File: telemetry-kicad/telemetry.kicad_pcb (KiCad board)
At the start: 4 copper layers, 0 parts

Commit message: Begun placement, need to make a footprint for the SD card module. All other footprints are loaded. Routing considerations are not input, such as the impidence controlled antenna trace.
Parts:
- added C1: 100nF, Capacitor_SMD:C_0805_2012Metric_Pad1.18x1.45mm_HandSolder, F.Cu at (128.3, 98.5)
- added C10: 1uF, Capacitor_SMD:C_0805_2012Metric_Pad1.18x1.45mm_HandSolder, F.Cu at (144.1, 98.5)
- added C12: 8pF, Capacitor_SMD:C_0805_2012Metric_Pad1.18x1.45mm_HandSolder, F.Cu at (123.2, 37.2)
- added C13: 8pF, Capacitor_SMD:C_0805_2012Metric_Pad1.18x1.45mm_HandSolder, F.Cu at (130.0, 44.5)
- added C15: 2.2uF, Capacitor_SMD:C_0805_2012Metric_Pad1.18x1.45mm_HandSolder, F.Cu at (172.2, 32.5)
- added C16: 2.2uF, Capacitor_SMD:C_0805_2012Metric_Pad1.18x1.45mm_HandSolder, F.Cu at (172.2, 35.5)
- added C17: 1uF, Capacitor_SMD:C_0805_2012Metric_Pad1.18x1.45mm_HandSolder, F.Cu at (132.5, 19.8)
- added C18: 1uF, Capacitor_SMD:C_0805_2012Metric_Pad1.18x1.45mm_HandSolder, F.Cu at (136.5, 19.7)
- added C19: 1uF, Capacitor_SMD:C_0805_2012Metric_Pad1.18x1.45mm_HandSolder, F.Cu at (140.5, 19.8)
- added C2: 10uF, Capacitor_SMD:C_0805_2012Metric_Pad1.18x1.45mm_HandSolder, F.Cu at (133.8, 98.5)
- added C20: 1uF, Capacitor_SMD:C_0805_2012Metric_Pad1.18x1.45mm_HandSolder, F.Cu at (144.5, 19.8)
- added C21: 1uF, Capacitor_SMD:C_0805_2012Metric_Pad1.18x1.45mm_HandSolder, F.Cu at (148.5, 19.8)
- added C22: 1uF, Capacitor_SMD:C_0805_2012Metric_Pad1.18x1.45mm_HandSolder, F.Cu at (152.5, 19.8)
- added C23: 10uF, Capacitor_SMD:C_0805_2012Metric_Pad1.18x1.45mm_HandSolder, F.Cu at (156.5, 19.8)
- added C24: 10uF, Capacitor_SMD:C_0805_2012Metric_Pad1.18x1.45mm_HandSolder, F.Cu at (160.4, 19.8)
- added C25: 10uF, Capacitor_SMD:C_0805_2012Metric_Pad1.18x1.45mm_HandSolder, F.Cu at (24.0, 112.0)
- added C26: 1uF, Capacitor_SMD:C_0805_2012Metric_Pad1.18x1.45mm_HandSolder, F.Cu at (28.0, 112.0)
- added C27: 1uF, Capacitor_SMD:C_0805_2012Metric_Pad1.18x1.45mm_HandSolder, F.Cu at (32.0, 112.0)
- added C28: 100nF, Capacitor_SMD:C_0805_2012Metric_Pad1.18x1.45mm_HandSolder, F.Cu at (52.8, 64.8)
- added C29: 100nF, Capacitor_SMD:C_0805_2012Metric_Pad1.18x1.45mm_HandSolder, F.Cu at (225.0, 45.8)
- added C3: 220nF, Capacitor_SMD:C_0805_2012Metric_Pad1.18x1.45mm_HandSolder, F.Cu at (138.6, 98.8)
- added C30: 10uF, Capacitor_SMD:C_0805_2012Metric_Pad1.18x1.45mm_HandSolder, F.Cu at (39.5, 112.0)
- added C31: 1uF, Capacitor_SMD:C_0805_2012Metric_Pad1.18x1.45mm_HandSolder, F.Cu at (43.5, 112.0)
- added C32: 1uF, Capacitor_SMD:C_0805_2012Metric_Pad1.18x1.45mm_HandSolder, F.Cu at (47.6, 112.0)
- added C33: 1uF, Capacitor_SMD:C_0805_2012Metric_Pad1.18x1.45mm_HandSolder, F.Cu at (210.0, 102.5)
- added C34: 100nF, Capacitor_SMD:C_0805_2012Metric_Pad1.18x1.45mm_HandSolder, F.Cu at (243.5, 79.0)
- added C5: 22uF, Capacitor_SMD:C_0805_2012Metric_Pad1.18x1.45mm_HandSolder, F.Cu at (129.1, 107.0)
- added C6: 22uF, Capacitor_SMD:C_0805_2012Metric_Pad1.18x1.45mm_HandSolder, F.Cu at (134.1, 107.0)
- added C7: 22uF, Capacitor_SMD:C_0805_2012Metric_Pad1.18x1.45mm_HandSolder, F.Cu at (138.6, 107.0)
- added C8: 10uF, Capacitor_SMD:C_0805_2012Metric_Pad1.18x1.45mm_HandSolder, F.Cu at (142.8, 107.0)
- added C9: 1uF, Capacitor_SMD:C_0805_2012Metric_Pad1.18x1.45mm_HandSolder, F.Cu at (147.1, 107.0)
- added D1: BZT52-C15S-AU_R1_000A1, Diode_SMD:D_SOD-123, F.Cu at (21.9, 53.5)
- added D2: D20V0L1B2LP-7B, Capacitor_SMD:C_0402_1005Metric_Pad0.74x0.62mm_HandSolder, F.Cu at (29.2, 49.0)
- added D4: PMEG2010BER, Diode_SMD:Nexperia_CFP3_SOD-123W, F.Cu at (103.8, 123.8)
- added F1: 1.5A Polyfuse, Inductor_SMD:L_1812_4532Metric_Pad1.30x3.40mm_HandSolder, F.Cu at (20.8, 45.8)
- added J1: 2601-1102, telemetry:WAGO-2601-1102, F.Cu at (38.5, 24.8)
- added J2: RFPC-SMA27-F, telemetry:RFPC-SMA27-F, F.Cu at (84.2, 23.8)
- added J4: 2601-1102, telemetry:WAGO-2601-1102, F.Cu at (50.9, 24.8)
- added J5: 2601-1102, telemetry:WAGO-2601-1102, F.Cu at (63.2, 24.8)
- added J6: USB_C_Receptacle_USB2.0_16P, telemetry:USB-C-SMD_TYPE-C-16PIN-2MD-073, F.Cu at (88.8, 124.4)
- added J8: TC2030, Connector:Tag-Connect_TC2030-IDC-NL_2x03_P1.27mm_Vertical, F.Cu at (60.6, 75.2)
- added L1: 8uH, 14m, Inductor_SMD:L_TaiTech_TMPC1265_13.5x12.5mm, F.Cu at (144.3, 87.0)
- added Q1: DMP3099LQ-7, Package_TO_SOT_SMD:SOT-23, F.Cu at (27.7, 42.2)
- added R1: 100k, Resistor_SMD:R_0805_2012Metric_Pad1.20x1.40mm_HandSolder, F.Cu at (154.1, 99.8)
- added R11: 10k, Resistor_SMD:R_0805_2012Metric_Pad1.20x1.40mm_HandSolder, F.Cu at (205.0, 119.0)
- added R12: 10k, Resistor_SMD:R_0805_2012Metric_Pad1.20x1.40mm_HandSolder, F.Cu at (205.0, 122.0)
- added R13: 10k, Resistor_SMD:R_0805_2012Metric_Pad1.20x1.40mm_HandSolder, F.Cu at (209.8, 110.2)
- added R14: 10k, Resistor_SMD:R_0805_2012Metric_Pad1.20x1.40mm_HandSolder, F.Cu at (209.8, 113.1)
- added R15: 10k, Resistor_SMD:R_0805_2012Metric_Pad1.20x1.40mm_HandSolder, F.Cu at (209.8, 116.0)
- added R16: 10k, Resistor_SMD:R_0805_2012Metric_Pad1.20x1.40mm_HandSolder, F.Cu at (209.8, 119.0)
- added R17: 5.1k, Resistor_SMD:R_0805_2012Metric_Pad1.20x1.40mm_HandSolder, F.Cu at (96.0, 111.2)
- added R18: 5.1k, Resistor_SMD:R_0805_2012Metric_Pad1.20x1.40mm_HandSolder, F.Cu at (95.9, 116.4)
- added R19: 10k, Resistor_SMD:R_0805_2012Metric_Pad1.20x1.40mm_HandSolder, F.Cu at (47.5, 65.8)
- added R2: 10K, Resistor_SMD:R_0805_2012Metric_Pad1.20x1.40mm_HandSolder, F.Cu at (21.0, 39.8)
- added R20: 10k, Resistor_SMD:R_0805_2012Metric_Pad1.20x1.40mm_HandSolder, F.Cu at (220.5, 38.8)
- added R21: 10k, Resistor_SMD:R_0805_2012Metric_Pad1.20x1.40mm_HandSolder, F.Cu at (214.5, 119.0)
- added R22: 10k, Resistor_SMD:R_0805_2012Metric_Pad1.20x1.40mm_HandSolder, F.Cu at (214.5, 122.0)
- added R23: 10k, Resistor_SMD:R_0805_2012Metric_Pad1.20x1.40mm_HandSolder, F.Cu at (220.5, 45.8)
- added R24: 10k, Resistor_SMD:R_0805_2012Metric_Pad1.20x1.40mm_HandSolder, F.Cu at (225.2, 38.8)
- added R25: 10k, Resistor_SMD:R_0805_2012Metric_Pad1.20x1.40mm_HandSolder, F.Cu at (248.8, 73.2)
- added R26: 10k, Resistor_SMD:R_0805_2012Metric_Pad1.20x1.40mm_HandSolder, F.Cu at (247.2, 93.5)
- added R27: 10k, Resistor_SMD:R_0805_2012Metric_Pad1.20x1.40mm_HandSolder, F.Cu at (248.8, 79.2)
- added R4: 43.2k, Resistor_SMD:R_0805_2012Metric_Pad1.20x1.40mm_HandSolder, F.Cu at (154.1, 105.8)
- added SW1: SW_NRST, telemetry:SMD-Switch, F.Cu at (53.3, 74.8)
- added SW2: SW_BOOT0, telemetry:SMD-Switch, F.Cu at (53.3, 79.0)
- added TP1: PG_BUCK, TestPoint:TestPoint_Pad_D1.0mm, F.Cu at (128.9, 88.5)
- added TP2: VBUS, TestPoint:TestPoint_Pad_D1.0mm, F.Cu at (125.5, 87.0)
- added TP3: +3V3, TestPoint:TestPoint_Pad_D1.0mm, F.Cu at (132.0, 88.5)
- added TP4: CANH1, TestPoint:TestPoint_Pad_D1.0mm, F.Cu at (221.2, 30.2)
- added TP5: CANL1, TestPoint:TestPoint_Pad_D1.0mm, F.Cu at (226.5, 30.2)
- added TP6: CANH2, TestPoint:TestPoint_Pad_D1.0mm, F.Cu at (241.2, 86.8)
- added TP7: CANL2, TestPoint:TestPoint_Pad_D1.0mm, F.Cu at (246.5, 86.8)
- added TP8: GND, TestPoint:TestPoint_Pad_D1.0mm, F.Cu at (33.5, 53.5)
- added U1: LMR33630ADDA, Package_SO:Texas_HSOP-8-1EP_3.9x4.9mm_P1.27mm_ThermalVias, F.Cu at (164.1, 92.1)
- added U2: TCAN337, Package_SO:SOIC-8_3.9x4.9mm_P1.27mm, F.Cu at (233.5, 38.2)
- added U3: TCAN337, Package_SO:SOIC-8_3.9x4.9mm_P1.27mm, F.Cu at (255.8, 87.0)
- added U4: ASM330LHHXG1TR, telemetry:ASM330LHHXG1TR, F.Cu at (27.8, 118.5)
- added U5: MAX-M10S-00B, telemetry:MAX-M10S-00B, F.Cu at (41.8, 124.2)
- added U7: STM32H523RCT7, telemetry:STM32H523RCT7, F.Cu at (146.5, 33.9)
- added U9: USBLC6-2SC6, Package_TO_SOT_SMD:SOT-23-6, F.Cu at (87.1, 112.3)
- added Y1: ABM8AIG-24.000MHz-8-2Z-T, telemetry:ABM8AIG-24.000MHZ-8-2Z-T, F.Cu at (129.7, 36.1)

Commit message: Progress on layout
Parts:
- moved C16 30.2 mm to (144.0, 24.8), turned to 90 degrees
- moved C24 27.8 mm to (144.8, 42.8), turned to -90 degrees
- moved C22 25.4 mm to (139.8, 41.8), turned to -90 degrees
- moved C15 25.4 mm to (149.2, 43.2), turned to -90 degrees
- moved C21 23.8 mm to (142.5, 42.8), turned to -90 degrees
- moved C20 23.0 mm to (153.2, 41.0)
- moved L1 20.2 mm to (163.8, 81.5), turned to 180 degrees
- moved C1 15.6 mm to (143.8, 101.0)
- moved C10 15.6 mm to (159.5, 101.0)
- moved C2 15.6 mm to (149.2, 101.0)
- moved C3 15.6 mm to (154.0, 101.2)
- moved C5 15.6 mm to (144.5, 109.5)
- moved C6 15.6 mm to (149.5, 109.5)
- moved C7 15.6 mm to (154.0, 109.5)
- moved C8 15.6 mm to (158.2, 109.5)
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
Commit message: Layout progress
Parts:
- moved C1 30.3 mm to (171.8, 89.5), turned to 90 degrees
- moved C5 27.3 mm to (152.0, 83.2), turned to 180 degrees
- moved C6 24.4 mm to (152.0, 85.2), turned to 180 degrees
- moved C7 22.3 mm to (152.0, 87.2), turned to 180 degrees
- moved C9 20.4 mm to (155.5, 90.3), turned to -90 degrees
- moved C8 19.9 mm to (153.2, 90.3), turned to 90 degrees
- moved TP1 17.3 mm to (143.4, 73.8)
- moved TP2 17.3 mm to (140.0, 72.2)
- moved TP3 17.3 mm to (146.5, 73.8)
- moved C10 14.4 mm to (172.0, 93.8)
- moved R4 12.6 mm to (165.8, 96.2), turned to 180 degrees
- moved C2 8.33 mm to (155.5, 95.5), turned to 90 degrees
- moved C3 6.86 mm to (157.8, 95.5), turned to 90 degrees
- moved R1 5.06 mm to (168.8, 97.2), turned to 90 degrees

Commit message: Routing progress
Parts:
- TP1, TP2, TP3, TP4, TP5, TP6, TP7, TP8: footprint TestPoint:TestPoint_Pad_D1.0mm -> TestPoint:TestPoint_THTPad_D2.0mm_Drill1.0mm
- moved U3 136.6 mm to (123.8, 51.5)
- moved R27 134.6 mm to (117.5, 49.0)
- moved C34 129.2 mm to (117.5, 52.5)
- moved TP6 126.5 mm to (121.0, 47.2)
- moved TP7 126.5 mm to (126.3, 47.2)
- moved R26 125.3 mm to (130.1, 49.2)
- moved R25 120.7 mm to (130.1, 53.0), turned to 180 degrees
- moved F1 118.8 mm to (120.2, 110.2), turned to -90 degrees
- moved R2 116.2 mm to (112.0, 112.0)
- moved D2 115.1 mm to (118.5, 116.8), turned to -90 degrees
- moved Q1 114.7 mm to (116.7, 114.5)
- moved D1 112.9 mm to (112.8, 115.8), turned to 90 degrees
- moved U2 109.8 mm to (123.8, 35.6)
- moved R24 106.8 mm to (117.5, 33.1)
- moved C29 106.6 mm to (117.5, 36.6)
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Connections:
- R23 pad 1: (no net) -> SIL_CAN1
- R23 pad 2: (no net) -> GND
- Y1 pad 2: (no net) -> GND
- Y1 pad 4: (no net) -> GND
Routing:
- net +3.3V: track 0.00 -> 57.0 mm
- net VBUS_USB: track 0.00 -> 14.7 mm, vias 0 -> 1
- net CYST_IN: track 0.00 -> 8.15 mm
- net CYST_OUT: track 0.00 -> 6.35 mm
- net Net-(U1-BOOT): track 0.00 -> 4.57 mm
- net /FB_BUCK: track 0.00 -> 4.25 mm
- net /VCC_BUCK: track 0.00 -> 4.13 mm
- net Net-(U1-PG): track 0.00 -> 3.67 mm
- net Net-(C15-Pad1): track 0.00 -> 2.75 mm
- net Net-(C16-Pad1): track 0.00 -> 2.57 mm
- added copper zone on F.Cu, net +3.3V
- added copper zone on F.Cu, net /SW_BUCK

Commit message: Routing Progressed, used Kicad MCP to make schematic for SD card
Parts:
- removed C32, C33: 1uF, Capacitor_SMD:C_0805_2012Metric_Pad1.18x1.45mm_HandSolder
- removed C34: 100nF, Capacitor_SMD:C_0805_2012Metric_Pad1.18x1.45mm_HandSolder
- removed D4: PMEG2010BER, Diode_SMD:Nexperia_CFP3_SOD-123W
- removed J8: TC2030, Connector:Tag-Connect_TC2030-IDC-NL_2x03_P1.27mm_Vertical
- removed R12, R13, R21, R22, R23, R24, R25, R26, R27: 10k, Resistor_SMD:R_0805_2012Metric_Pad1.20x1.40mm_HandSolder
- removed U9: USBLC6-2SC6, Package_TO_SOT_SMD:SOT-23-6
- added C11: 8pF, Capacitor_SMD:C_0805_2012Metric_Pad1.18x1.45mm_HandSolder, F.Cu at (88.5, 94.8)
- added C14: 2.2uF, Capacitor_SMD:C_0805_2012Metric_Pad1.18x1.45mm_HandSolder, F.Cu at (80.8, 108.2)
- added C4: 22uF, Capacitor_SMD:C_0805_2012Metric_Pad1.18x1.45mm_HandSolder, F.Cu at (118.5, 103.5)
- added D3: PMEG2010BER, Diode_SMD:Nexperia_CFP3_SOD-123W, F.Cu at (96.8, 124.8)
- added J3: TC2030, Connector:Tag-Connect_TC2030-IDC-NL_2x03_P1.27mm_Vertical, F.Cu at (77.5, 142.1)
- added J7: SD_Card_Receptacle, telemetry:SD_Yamaichi_FPS009-4200-0, F.Cu at (265.9, 119.0)
- added R10: 5.1k, Resistor_SMD:R_0805_2012Metric_Pad1.20x1.40mm_HandSolder, F.Cu at (83.5, 119.8)
- added R3: 43.2k, Resistor_SMD:R_0805_2012Metric_Pad1.20x1.40mm_HandSolder, F.Cu at (135.0, 117.8)
- added R5: 10k, Resistor_SMD:R_0805_2012Metric_Pad1.20x1.40mm_HandSolder, F.Cu at (22.2, 114.0)
- added R6: 10k, Resistor_SMD:R_0805_2012Metric_Pad1.20x1.40mm_HandSolder, F.Cu at (28.0, 114.0)
- added R7: 10k, Resistor_SMD:R_0805_2012Metric_Pad1.20x1.40mm_HandSolder, F.Cu at (41.8, 155.4)
- added R8: 10k, Resistor_SMD:R_0805_2012Metric_Pad1.20x1.40mm_HandSolder, F.Cu at (41.8, 158.4)
- added R9: 10k, Resistor_SMD:R_0805_2012Metric_Pad1.20x1.40mm_HandSolder, F.Cu at (41.8, 161.3)
- added U6: TCAN337, Package_SO:SOIC-8_3.9x4.9mm_P1.27mm, F.Cu at (48.4, 157.5)
- C10: value 1uF -> 100nF
- C13: value 8pF -> 100nF
- C16: value 2.2uF -> 100nF
- C23, C30, C8: value 10uF -> 1uF
- C26: value 1uF -> 10uF
- C28: value 100nF -> 1uF
- C29: value 100nF -> 10uF
- C7: value 22uF -> 10uF
- R11: value 10k -> 5.1k
- R17, R18: value 5.1k -> 10k
- R4: value 43.2k -> 10k
- TP1: value PG_BUCK -> VBUS
- TP2: value VBUS -> +3V3
- TP3: value +3V3 -> PG_BUCK
- TP4: value CANH1 -> GND
- TP5: value CANL1 -> CANH1
- TP6: value CANH2 -> CANL1
- TP7: value CANL2 -> CANH2
- TP8: value GND -> CANL2
- U2: value TCAN337 -> ASM330LHHXG1TR; footprint Package_SO:SOIC-8_3.9x4.9mm_P1.27mm -> telemetry:ASM330LHHXG1TR
- U3: value TCAN337 -> MAX-M10S-00B; footprint Package_SO:SOIC-8_3.9x4.9mm_P1.27mm -> telemetry:MAX-M10S-00B
- U4: value ASM330LHHXG1TR -> TCAN337; footprint telemetry:ASM330LHHXG1TR -> Package_SO:SOIC-8_3.9x4.9mm_P1.27mm
- U5: value MAX-M10S-00B -> STM32H523RCT7; footprint telemetry:MAX-M10S-00B -> telemetry:STM32H523RCT7
- U7: value STM32H523RCT7 -> USBLC6-2SC6; footprint telemetry:STM32H523RCT7 -> Package_TO_SOT_SMD:SOT-23-6
- moved R19 201.7 mm to (221.8, 126.5)
- moved C26 156.4 mm to (162.8, 35.8)
- moved C27 153.0 mm to (161.8, 27.0)
- moved C28 150.4 mm to (167.5, 29.8)
- moved R4 139.8 mm to (26.0, 100.5)
- moved R17 137.0 mm to (222.0, 109.5), turned to 0 degrees
- moved C10 136.5 mm to (35.2, 101.8)
- moved R18 130.0 mm to (221.8, 129.0), turned to 0 degrees
- moved C17 129.3 mm to (221.8, 119.5), turned to 180 degrees
- moved R11 111.8 mm to (93.2, 119.8)
- moved R20 105.9 mm to (28.8, 68.2)
- moved C30 98.3 mm to (113.5, 72.5)
- moved C31 98.3 mm to (113.5, 70.2)
- moved C16 82.2 mm to (22.0, 68.2)
- moved C13 74.2 mm to (59.5, 157.0)
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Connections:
- C10 pad 1: /VCC_BUCK -> GND
- C10 pad 2: GND -> +3.3V
- C12 pad 1: CYST_OUT -> CYST_IN
- C13 pad 1: CYST_IN -> GND
- C13 pad 2: GND -> +3.3V
- C16 pad 1: Net-(C16-Pad1) -> NRST
- C25 pad 1: GND -> +3.3V
- C25 pad 2: +3.3V -> GND
- C26 pad 1: +3.3V -> GND
- C26 pad 2: GND -> +3.3V
- C28 pad 1: NRST -> +3.3V
- C30 pad 1: GND -> +3.3V
- C30 pad 2: +3.3V -> GND
- C7 pad 1: +3.3V -> GND
- C7 pad 2: GND -> +3.3V
- C8 pad 1: GND -> +3.3V
- C8 pad 2: +3.3V -> GND
- C9 pad 1: +3.3V -> /VCC_BUCK
- J4 pad 1: Net-(J4-1_1) -> /CANH1
- J4 pad 2: Net-(J4-1_1) -> /CANH1
- J4 pad 3: Net-(J4-2_1) -> /CANL1
- J4 pad 4: Net-(J4-2_1) -> /CANL1
- J5 pad 1: Net-(J5-1_1) -> /CANH2
- J5 pad 2: Net-(J5-1_1) -> /CANH2
- J5 pad 3: Net-(J5-2_1) -> /CANL2
- J5 pad 4: Net-(J5-2_1) -> /CANL2
- R11 pad 1: +3.3V -> Net-(J6-CC2)
- R11 pad 2: CMD_SD -> GND
- R14 pad 2: D2_SD -> CMD_SD
- R15 pad 2: D1_SD -> CLK_SD
- R16 pad 2: D0_SD -> D3_SD
- R17 pad 1: Net-(J6-CC1) -> +3.3V
- R17 pad 2: GND -> D2_SD
- R18 pad 1: Net-(J6-CC2) -> +3.3V
- R18 pad 2: GND -> D1_SD
- R19 pad 1: Net-(U7A-BOOT0) -> +3.3V
- R19 pad 2: GND -> D0_SD
- R20 pad 1: +3.3V -> Net-(U5A-BOOT0)
- R20 pad 2: FLT_CAN1 -> GND
- R4 pad 1: /FB_BUCK -> +3.3V
- R4 pad 2: GND -> TXD_CAN1
- SW2 pad 1: Net-(U7A-BOOT0) -> Net-(U5A-BOOT0)
- TP1 pad 1: Net-(U1-PG) -> VBUS_USB
- TP2 pad 1: VBUS_USB -> +3.3V
- TP3 pad 1: +3.3V -> Net-(U1-PG)
- TP4 pad 1: Net-(J4-1_1) -> GND
- TP5 pad 1: Net-(J4-2_1) -> /CANH1
- TP6 pad 1: Net-(J5-1_1) -> /CANL1
- TP7 pad 1: Net-(J5-2_1) -> /CANH2
- TP8 pad 1: GND -> /CANL2
- U2 pad 1: TXD_CAN1 -> DO_IMU
- U2 pad 3: +3.3V -> GND
- U2 pad 4: RXD_CAN1 -> INT1
- U2 pad 5: FLT_CAN1 -> +3.3V
- U2 pad 6: Net-(J4-2_1) -> GND
- U2 pad 7: Net-(J4-1_1) -> GND
- U2 pad 8: SIL_CAN1 -> +3.3V
- U3 pad 1: TXD_CAN2 -> GND
- U3 pad 2: GND -> TXD_GNSS
- U3 pad 3: +3.3V -> RXD_GNSS
- U3 pad 4: RXD_CAN2 -> TIMEPULSE_GNSS
- U3 pad 5: FLT_CAN2 -> unconnected-(U3-EXTINT-Pad5)
- U3 pad 6: Net-(J5-2_1) -> unconnected-(U3-V_BCKP-Pad6)
- U3 pad 7: Net-(J5-1_1) -> +3.3V
- U3 pad 8: SIL_CAN2 -> +3.3V
- U4 pad 1: DO_IMU -> TXD_CAN1
- U4 pad 3: GND -> +3.3V
- U4 pad 4: INT1 -> RXD_CAN1
- U4 pad 5: +3.3V -> FLT_CAN1
- U4 pad 6: GND -> /CANL1
- U4 pad 7: GND -> /CANH1
- U4 pad 8: +3.3V -> SIL_CAN1
- U5 pad 1: GND -> +3.3V
- U5 pad 10: GND -> unconnected-(U5A-PC2-Pad10)
- U5 pad 11: ANT -> unconnected-(U5A-PC3-Pad11)
- U5 pad 13: unconnected-(U5-LNA_EN-Pad13) -> +3.3V
- U5 pad 18: unconnected-(U5-~{SAFEBOOT}-Pad18) -> GND
- U5 pad 2: TXD_GNSS -> unconnected-(U5A-PC13-Pad2)
- U5 pad 3: RXD_GNSS -> unconnected-(U5A-PC14-OSC32_IN-Pad3)
- U5 pad 4: TIMEPULSE_GNSS -> unconnected-(U5A-PC15-OSC32_OUT-Pad4)
- U5 pad 5: unconnected-(U5-EXTINT-Pad5) -> CYST_IN
- U5 pad 6: unconnected-(U5-V_BCKP-Pad6) -> CYST_OUT
- U5 pad 7: +3.3V -> NRST
- U5 pad 8: +3.3V -> unconnected-(U5A-PC0-Pad8)
- U7 pad 1: +3.3V -> /inD-
- U7 pad 2: unconnected-(U7A-PC13-Pad2) -> GND
- U7 pad 3: unconnected-(U7A-PC14-OSC32_IN-Pad3) -> /inD+
- U7 pad 4: unconnected-(U7A-PC15-OSC32_OUT-Pad4) -> D+
- U7 pad 5: CYST_IN -> /VBUS
- U7 pad 6: CYST_OUT -> D-
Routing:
- net /VBUS: track 0.00 -> 26.7 mm
- net Net-(D2-A1): track 0.00 -> 8.81 mm
- net +3.3V: track 57.0 -> 48.8 mm
- net VBUS_USB: track 14.7 -> 22.7 mm
- net Net-(D1-A): track 0.00 -> 7.74 mm
- net /inD-: track 0.00 -> 6.30 mm
- net /inD+: track 0.00 -> 6.26 mm
- net D-: track 0.00 -> 6.16 mm
- net D+: track 0.00 -> 5.35 mm
- net Net-(J6-CC1): track 0.00 -> 4.41 mm, vias 0 -> 2
- net Net-(J6-CC2): track 0.00 -> 3.85 mm, vias 0 -> 2
- net Net-(C16-Pad1): track 2.57 -> 0.00 mm
- net Net-(C14-Pad1): track 0.00 -> 2.52 mm

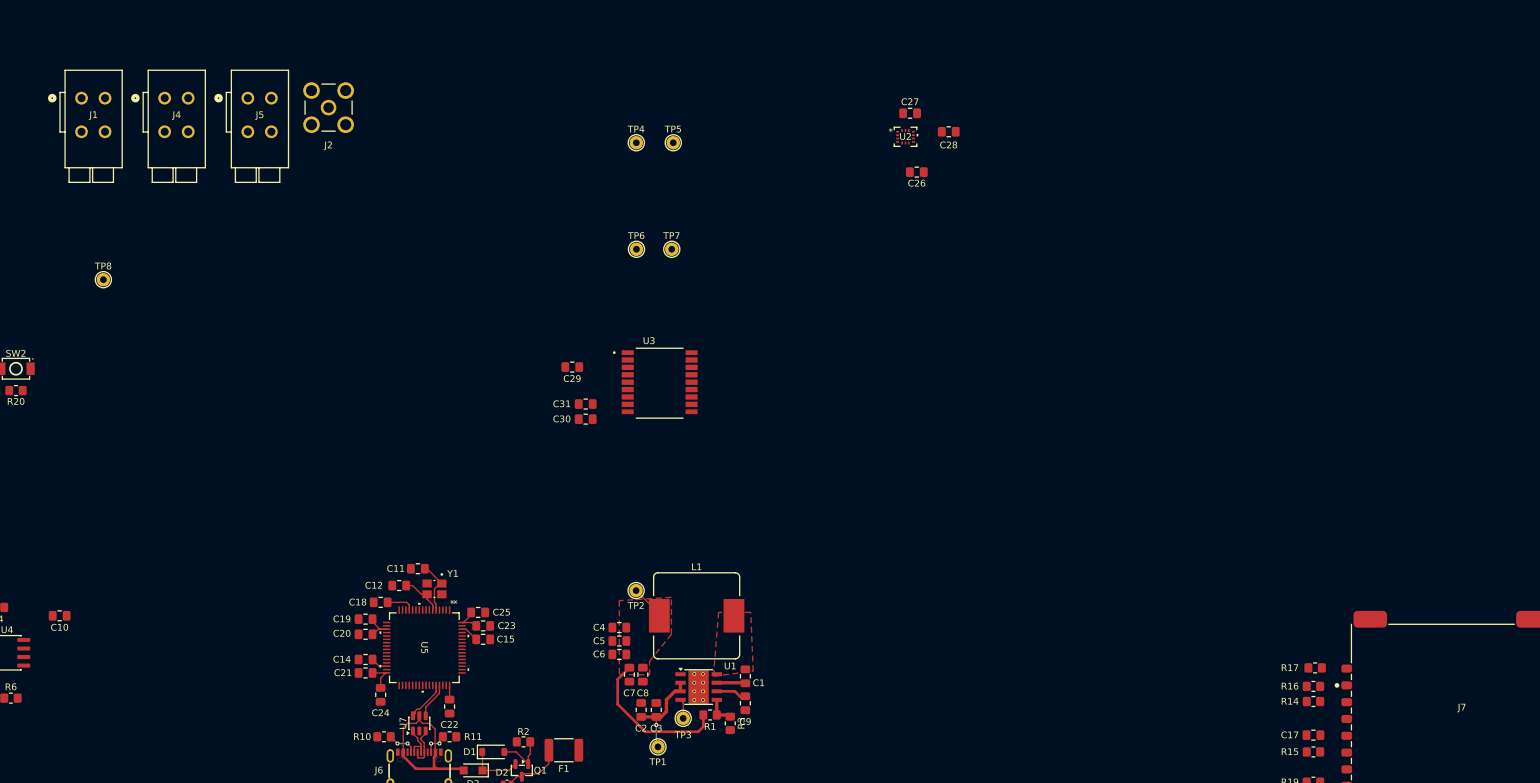
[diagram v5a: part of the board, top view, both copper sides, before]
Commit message: Added indicating LEDs
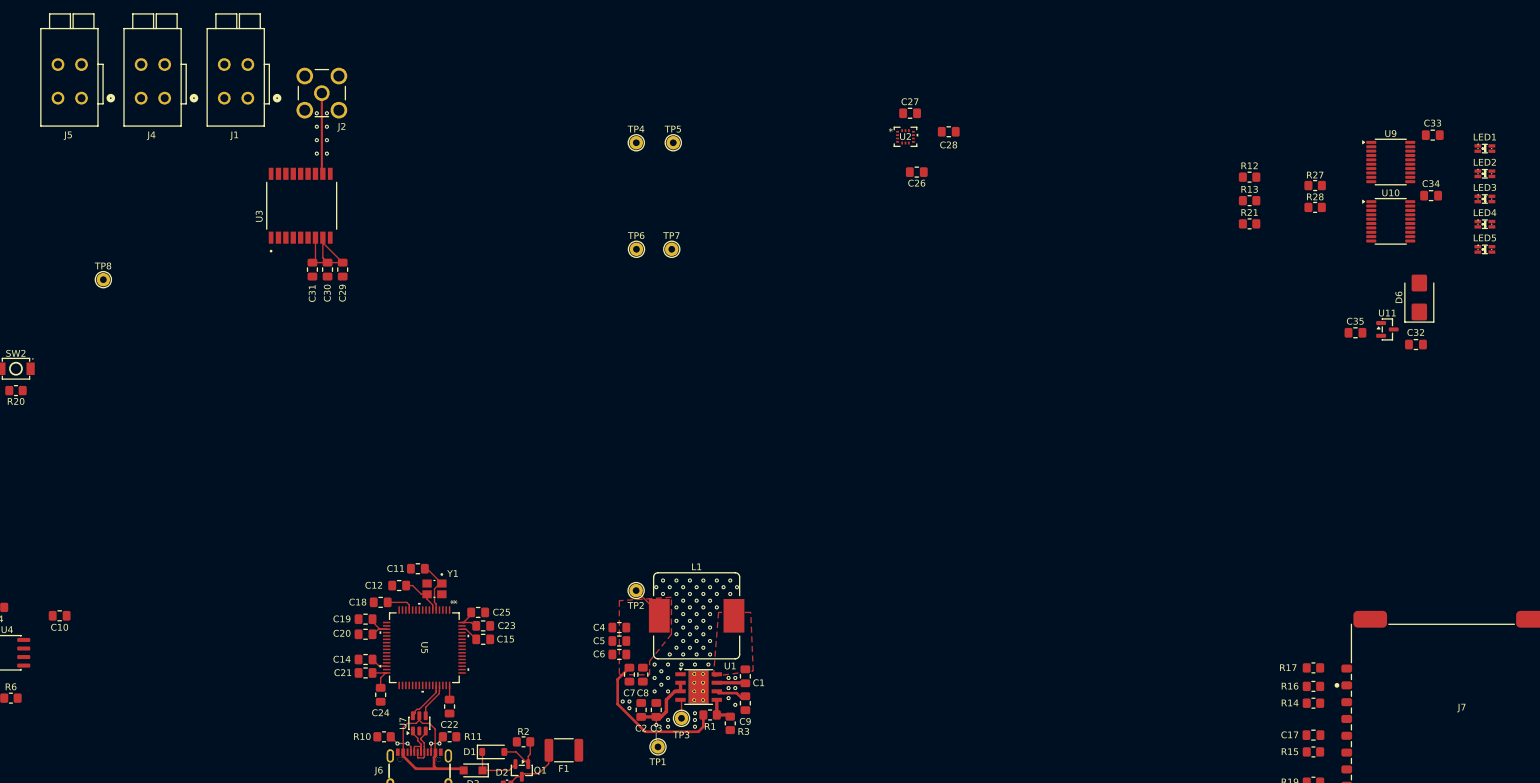
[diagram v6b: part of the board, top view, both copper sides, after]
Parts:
- added C32: 1uF, Capacitor_SMD:C_0805_2012Metric_Pad1.18x1.45mm_HandSolder, F.Cu at (237.0, 61.4)
- added C33: 100nF, Capacitor_SMD:C_0805_2012Metric_Pad1.18x1.45mm_HandSolder, F.Cu at (239.5, 30.2)
- added C34: 100nF, Capacitor_SMD:C_0805_2012Metric_Pad1.18x1.45mm_HandSolder, F.Cu at (239.2, 39.2)
- added C35: 1uF, Capacitor_SMD:C_0805_2012Metric_Pad1.18x1.45mm_HandSolder, F.Cu at (228.0, 59.6)
- added D6: SMBJ16A, telemetry:SMBJ16A, F.Cu at (237.5, 54.4)
- added LED1: XL-2012SURUGC, telemetry:LED-SMD_4P-L2.0-W1.3-RD-TL, F.Cu at (247.2, 32.2)
- added LED2: XL-2012SURUGC, telemetry:LED-SMD_4P-L2.0-W1.3-RD-TL, F.Cu at (247.2, 36.0)
- added LED3: XL-2012SURUGC, telemetry:LED-SMD_4P-L2.0-W1.3-RD-TL, F.Cu at (247.2, 39.8)
- added LED4: XL-2012SURUGC, telemetry:LED-SMD_4P-L2.0-W1.3-RD-TL, F.Cu at (247.2, 43.5)
- added LED5: XL-2012SURUGC, telemetry:LED-SMD_4P-L2.0-W1.3-RD-TL, F.Cu at (247.2, 47.2)
- added R12: 10K, Resistor_SMD:R_0805_2012Metric_Pad1.20x1.40mm_HandSolder, F.Cu at (212.2, 36.5)
- added R13: 4.7k, Resistor_SMD:R_0805_2012Metric_Pad1.20x1.40mm_HandSolder, F.Cu at (212.2, 40.0)
- added R21: 4.7k, Resistor_SMD:R_0805_2012Metric_Pad1.20x1.40mm_HandSolder, F.Cu at (212.2, 43.5)
- added R27: 1.1k, Resistor_SMD:R_0805_2012Metric_Pad1.20x1.40mm_HandSolder, F.Cu at (222.0, 37.8)
- added R28: 3.74k, Resistor_SMD:R_0805_2012Metric_Pad1.20x1.40mm_HandSolder, F.Cu at (222.0, 41.0)
- added U10: TLC59108IPWR, telemetry:TLC59108IPWR, F.Cu at (233.2, 43.1)
- added U11: MCP1703T-5002E/CB, telemetry:MCP1703T-5002E-CB, F.Cu at (232.8, 59.1)
- added U9: TLC59108IPWR, telemetry:TLC59108IPWR, F.Cu at (233.2, 34.2)
- U1: value LMR33630ADDA -> LMR33610ADDAR
- moved U3 59.5 mm to (71.1, 40.8), turned to 90 degrees
- moved C31 45.3 mm to (72.8, 50.2), turned to -90 degrees
- moved C30 44.4 mm to (75.1, 50.2), turned to -90 degrees
- moved C29 37.1 mm to (77.3, 50.2), turned to 90 degrees
- moved J2 2.38 mm to (74.2, 24.0)
- moved R14 0.25 mm to (221.8, 114.8)
- moved R17 0.25 mm to (221.8, 109.5)
- moved TP3 0.25 mm to (127.8, 117.0)
- turned J1 to 180 degrees
- turned J4 to 180 degrees
- turned J5 to 180 degrees
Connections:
- U5 pad 41: unconnected-(U5A-PA8-Pad41) -> SCL_LED
- U5 pad 56: unconnected-(U5A-PB4-Pad56) -> SDA_LED
- U5 pad 57: unconnected-(U5A-PB5-Pad57) -> RST_LED
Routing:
- net +3.3V: track 48.8 -> 66.1 mm
- net ANT: track 0.00 -> 12.1 mm
- net Net-(U1-PG): track 3.67 -> 2.81 mm
- net GND: vias 0 -> 33
- net (no net): vias 0 -> 48
